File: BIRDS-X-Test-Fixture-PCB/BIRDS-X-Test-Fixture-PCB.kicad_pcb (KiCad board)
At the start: 2 copper layers, 97.3 x 99.3 mm, 34 parts, among them J101 LPC-50M2LG, J102 Conn_01x05, J105 Conn_01x06, J109 Conn_01x05, J110 Conn_02x05_Odd_Even, J111 Conn_02x05_Odd_Even

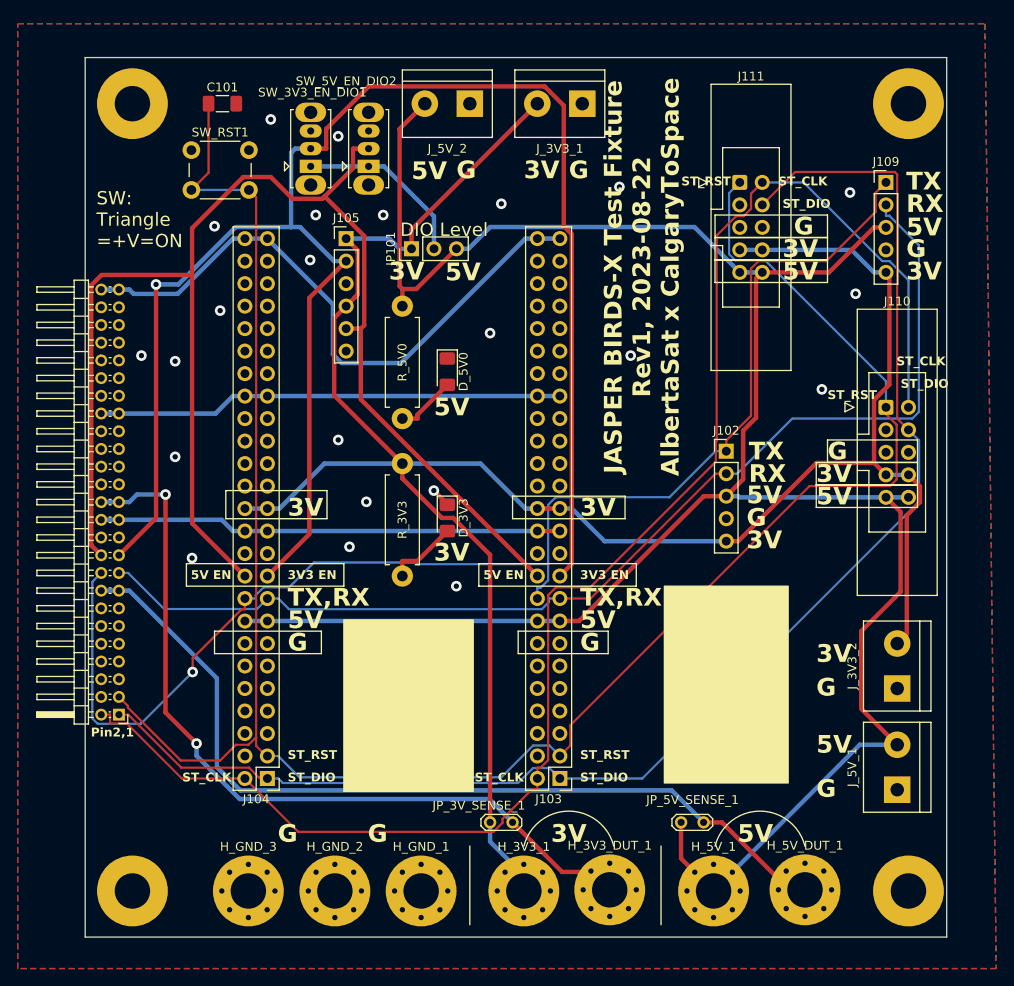
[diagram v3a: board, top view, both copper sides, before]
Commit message: Update test fixture board
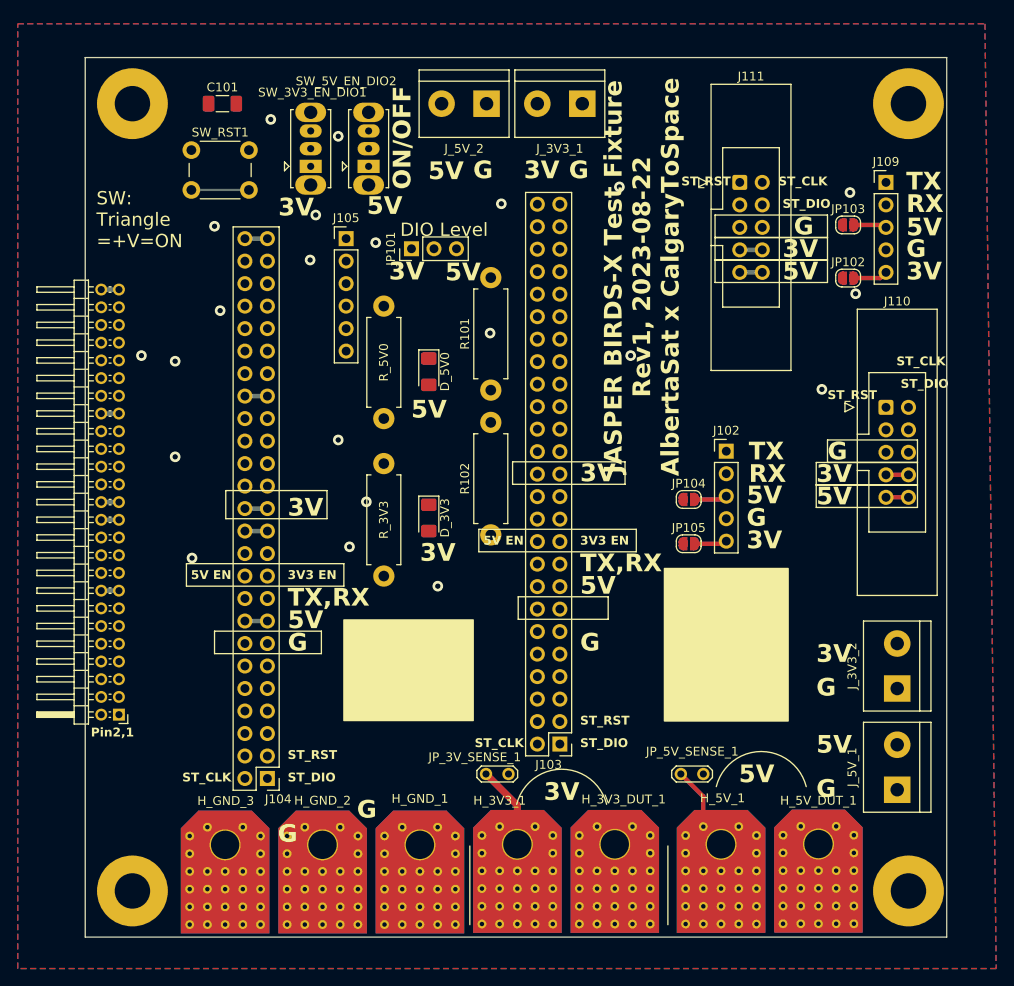
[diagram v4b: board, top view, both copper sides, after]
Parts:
- added JP102: SolderJumper_2_Open, Jumper:SolderJumper-2_P1.3mm_Open_RoundedPad1.0x1.5mm, F.Cu at (162.3, 63.0)
- added JP103: SolderJumper_2_Open, Jumper:SolderJumper-2_P1.3mm_Open_RoundedPad1.0x1.5mm, F.Cu at (162.3, 57.0)
- added JP104: SolderJumper_2_Open, Jumper:SolderJumper-2_P1.3mm_Open_RoundedPad1.0x1.5mm, F.Cu at (144.3, 88.0)
- added JP105: SolderJumper_2_Open, Jumper:SolderJumper-2_P1.3mm_Open_RoundedPad1.0x1.5mm, F.Cu at (144.3, 93.0)
- added R101: 1k, Resistor_THT:R_Axial_DIN0411_L9.9mm_D3.6mm_P12.70mm_Horizontal, F.Cu at (122.0, 75.7)
- added R102: 1k, Resistor_THT:R_Axial_DIN0411_L9.9mm_D3.6mm_P12.70mm_Horizontal, F.Cu at (122.0, 92.0)
- H_3V3_1, H_3V3_DUT_1, H_5V_1, H_5V_DUT_1, H_GND_1, H_GND_2, H_GND_3: footprint MountingHole:MountingHole_4mm_Pad_Via -> 0TestFixtureFootprintLib:EdgeAlligatorConnector
- moved H_GND_3 9.57 mm to (92.0, 123.0)
- moved H_GND_2 9.31 mm to (103.0, 123.0)
- moved H_5V_1 9.31 mm to (148.0, 122.9)
- moved H_5V_DUT_1 9.30 mm to (159.0, 122.9)
- moved H_3V3_1 9.30 mm to (125.0, 122.9)
- moved H_GND_1 9.21 mm to (114.0, 123.0)
- moved H_3V3_DUT_1 9.16 mm to (136.0, 122.9)
- moved JP_3V_SENSE_1 5.48 mm to (124.0, 119.0)
- moved JP_5V_SENSE_1 5.46 mm to (146.0, 119.0)
- moved J103 3.88 mm to (129.8, 115.6)
- moved D_3V3 2.09 mm to (115.0, 90.1)
- moved D_5V0 2.09 mm to (115.0, 73.6)
- moved R_3V3 2.09 mm to (109.9, 83.9)
- moved R_5V0 2.09 mm to (109.9, 66.2)
- moved J_5V_2 1.89 mm to (121.5, 43.3)
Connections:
- J102 pad 3: SUP_5V0 -> Net-(J102-Pin_3)
- J102 pad 5: SUP_3V3_2 -> Net-(J102-Pin_5)
- J109 pad 3: SUP_5V0 -> Net-(J109-Pin_3)
- J109 pad 5: SUP_3V3_2 -> Net-(J109-Pin_5)
- SW_3V3_EN_DIO1 pad 1: Net-(JP101-C) -> Net-(SW_3V3_EN_DIO1-A)
- SW_5V_EN_DIO2 pad 1: Net-(JP101-C) -> Net-(SW_5V_EN_DIO2-A)
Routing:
- net SUP_5V0: track 276.6 -> 14.6 mm
- net SUP_3V3_2: track 276.9 -> 20.1 mm
- net ST_RST: track 233.7 -> 6.50 mm
- net DIO1_3V3_EN_FROM_BOSS: track 195.8 -> 0.00 mm, vias 1 -> 0
- net ST_SWDCLK: track 175.0 -> 0.00 mm
- net DIO2_5V_EN_FROM_BOSS: track 166.3 -> 0.00 mm
- net ST_SWDIO: track 162.5 -> 0.00 mm
- net /UART_TX_JASPER_TO_BOSS: track 154.3 -> 0.00 mm, vias 1 -> 0
- net /UART_RX_BOSS_TO_JASPER: track 127.6 -> 0.00 mm
- net /5V_DUT: track 115.7 -> 2.00 mm
- net /3V3_DUT: track 108.0 -> 2.00 mm, vias 2 -> 0
- net SUP_3V3_1: track 69.5 -> 4.54 mm
- net SUP_UNREG_2: track 52.6 -> 4.54 mm
- net SUP_UNREG_1: track 52.3 -> 4.54 mm
- net Net-(JP101-C): track 19.9 -> 0.00 mm
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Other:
- board text added: "ON/OFF"

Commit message: Finish routing test fixture board
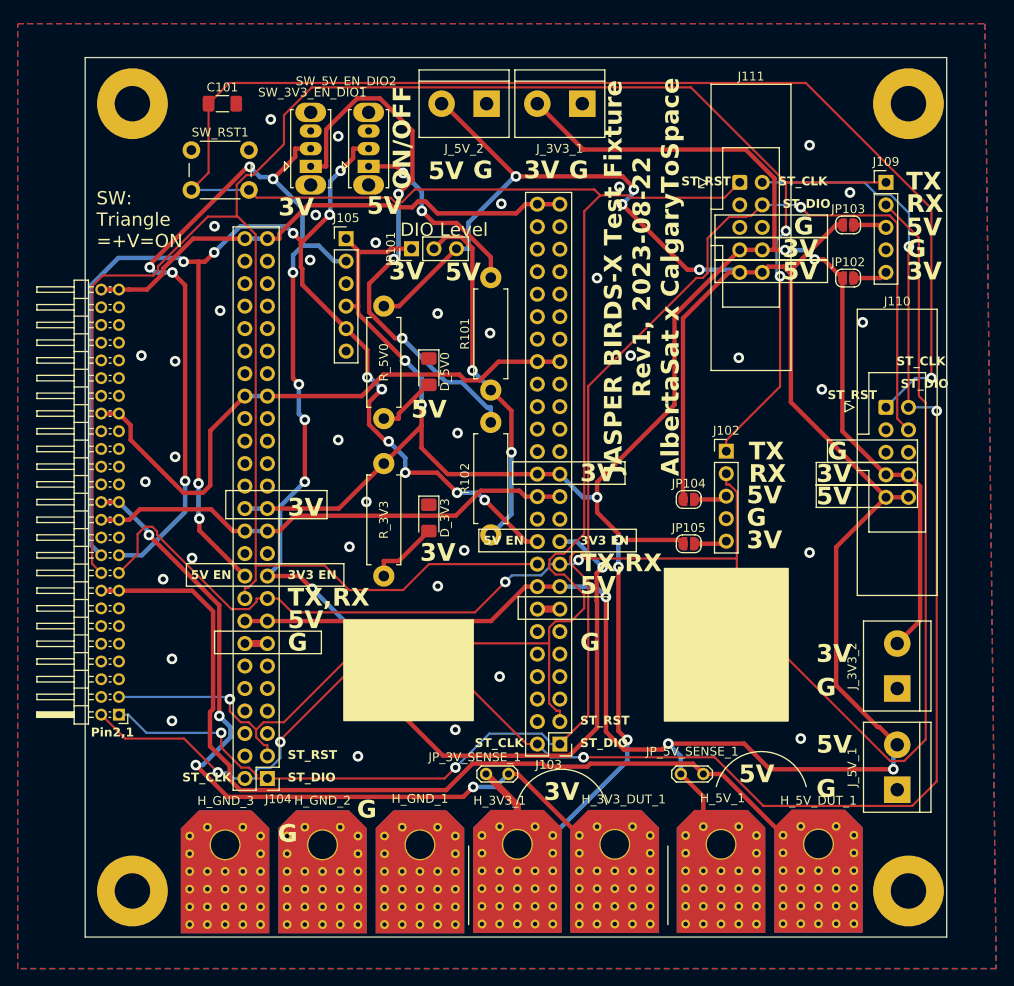
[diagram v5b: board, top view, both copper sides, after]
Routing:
- net SUP_5V0: track 14.6 -> 336.9 mm, vias 0 -> 7
- net ST_RST: track 6.50 -> 315.5 mm, vias 0 -> 2
- net SUP_3V3_2: track 20.1 -> 327.0 mm, vias 0 -> 8
- net /UART_TX_JASPER_TO_BOSS: track 0.00 -> 253.0 mm, vias 0 -> 2
- net ST_SWDCLK: track 0.00 -> 197.3 mm, vias 0 -> 5
- net DIO1_3V3_EN_FROM_BOSS: track 0.00 -> 193.9 mm, vias 0 -> 12
- net /UART_RX_BOSS_TO_JASPER: track 0.00 -> 189.0 mm, vias 0 -> 2
- net ST_SWDIO: track 0.00 -> 171.9 mm, vias 0 -> 3
- net DIO2_5V_EN_FROM_BOSS: track 0.00 -> 161.7 mm, vias 0 -> 13
- net /5V_DUT: track 2.00 -> 155.2 mm
- net /3V3_DUT: track 2.00 -> 141.4 mm, vias 0 -> 4
- net SUP_UNREG_2: track 4.54 -> 66.8 mm
- net Net-(SW_3V3_EN_DIO1-A): track 0.00 -> 61.0 mm, vias 0 -> 3
- net SUP_3V3_1: track 4.54 -> 57.7 mm
- net SUP_UNREG_1: track 4.54 -> 55.5 mm
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
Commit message: Touch up test fixture board
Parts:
- JP_3V_SENSE_1, JP_5V_SENSE_1: footprint TestPoint:TestPoint_2Pads_Pitch2.54mm_Drill0.8mm -> Connector_PinHeader_2.54mm:PinHeader_1x02_P2.54mm_Vertical
- moved H_GND_1 1.00 mm to (113.0, 123.0)
- moved JP_3V_SENSE_1 0.75 mm to (123.2, 119.0), turned to -90 degrees
- moved H_GND_2 0.50 mm to (102.5, 123.0)
- turned JP_5V_SENSE_1 to -90 degrees
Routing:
- net /5V_DUT: track 155.2 -> 158.1 mm
- net ST_SWDCLK: track 197.3 -> 198.0 mm
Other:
- board text added: "JASPER BIRDS-X Test Fixture Rev2, 2023-11-30 AlbertaSat x CalgaryToSpace"
- board text removed: "JASPER BIRDS-X Test Fixture Rev1, 2023-08-22 AlbertaSat x CalgaryToSpace"
